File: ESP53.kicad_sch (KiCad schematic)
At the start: 52 parts, among them IC1 ESP32-C5HR8, J2 Conn_02x04_Odd_Even, J3 USB_C_Receptacle_USB2.0_16P, SW1 SW_Push, SW2 SW_Push, U2 LN1134A332MR, Y1 48MHz

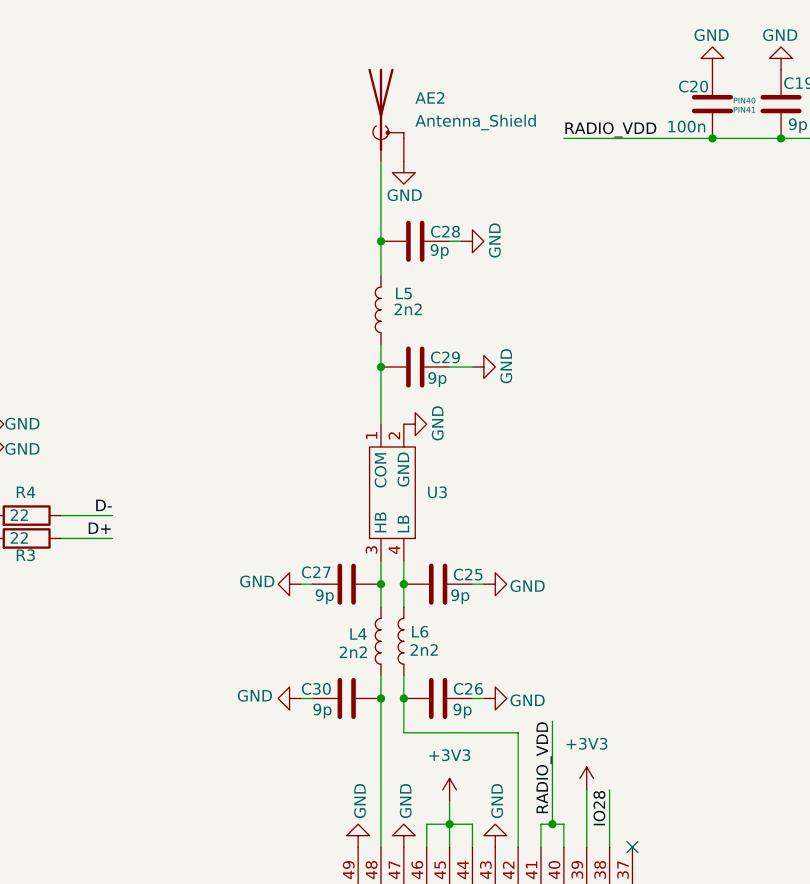
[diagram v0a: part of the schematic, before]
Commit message: update wifi connection routing
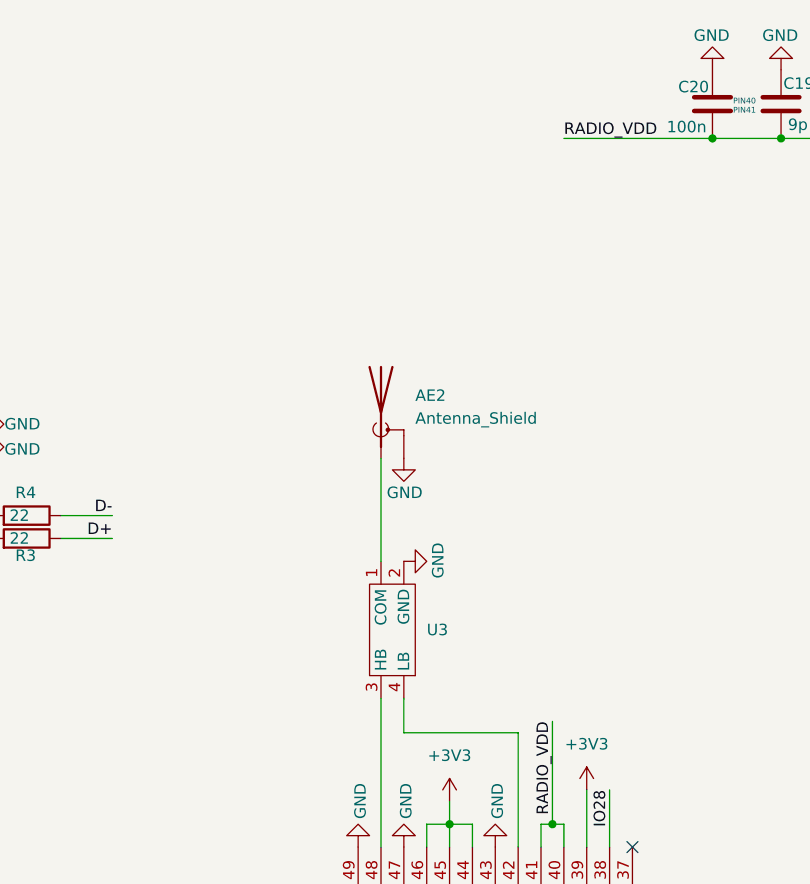
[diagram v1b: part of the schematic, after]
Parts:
- removed C25, C26, C27, C28, C29, C30: 9p, Resistor_SMD:R_0402_1005Metric, symbol Device:C
- removed L4, L5, L6: 2n2, Inductor_SMD:L_0402_1005Metric, symbol Device:L
- AE2: LCSC C201761 -> C3285113
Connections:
- net at IC1.48 (ANT_5G): now also U3.3 (HB)
- net at IC1.42 (ANT_2G): now also U3.4 (LB)
- net at AE2.1 (A): now also U3.1 (COM)
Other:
- moved on the sheet: AE2, U3
